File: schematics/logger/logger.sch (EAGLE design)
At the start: 21 parts

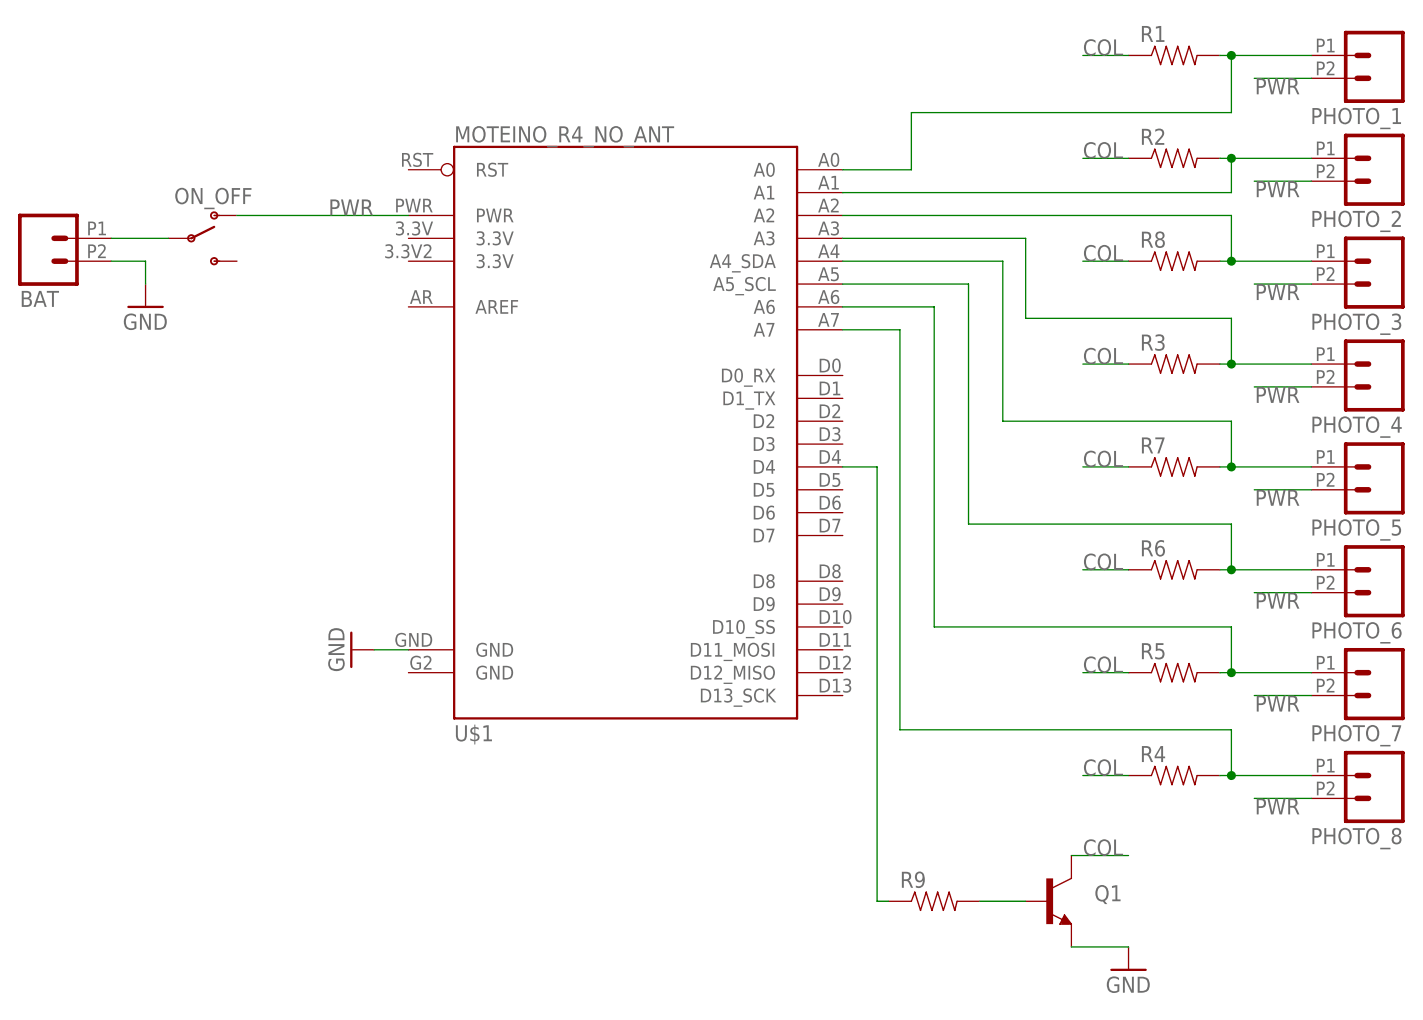
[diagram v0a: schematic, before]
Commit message: Changed photodiode power supply
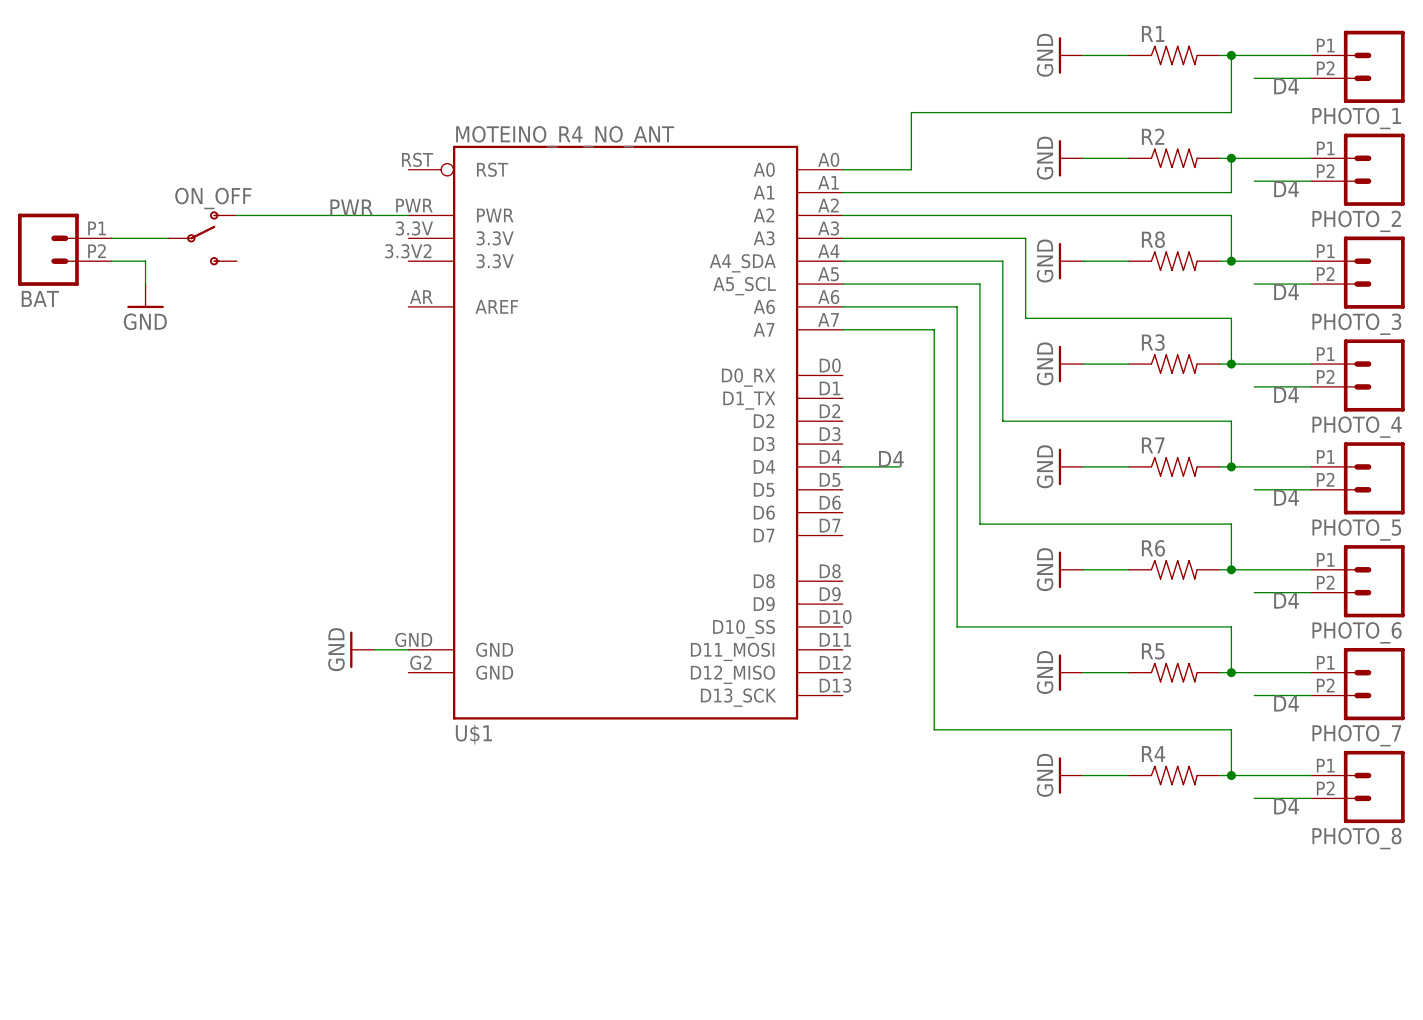
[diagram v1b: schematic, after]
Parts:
- removed Q1: (no value), SparkFun-DiscreteSemi:TRANSISTOR_NPN2N3904
- removed R9: (no value), SparkFun-Resistors:RESISTORPTH-1/4W
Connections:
- removed net COL: Q1.C, R1.1, R2.1, R3.1, R4.1, R5.1, R6.1, R7.1, R8.1
- removed net N$18: Q1.B, R9.2
- removed net N$19: R9.1, U$1.D4
- new net D4: PHOTO_1.2, PHOTO_2.2, PHOTO_3.2, PHOTO_4.2, PHOTO_5.2, PHOTO_6.2, PHOTO_7.2, PHOTO_8.2, U$1.D4
- new net N$6: R6.1
- net GND: now also R1.1, R2.1, R3.1, R4.1, R5.1, R7.1, R8.1; no longer Q1.E
- net PWR: no longer PHOTO_1.2, PHOTO_2.2, PHOTO_3.2, PHOTO_4.2, PHOTO_5.2, PHOTO_6.2, PHOTO_7.2, PHOTO_8.2
